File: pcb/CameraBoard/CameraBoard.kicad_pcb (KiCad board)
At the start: 2 copper layers, 17 parts, among them P2 CONN_01X03, P3 CONN_01X03, P4 CONN_01X08, U1 arduino_mini, U2 notgate_74HCT04

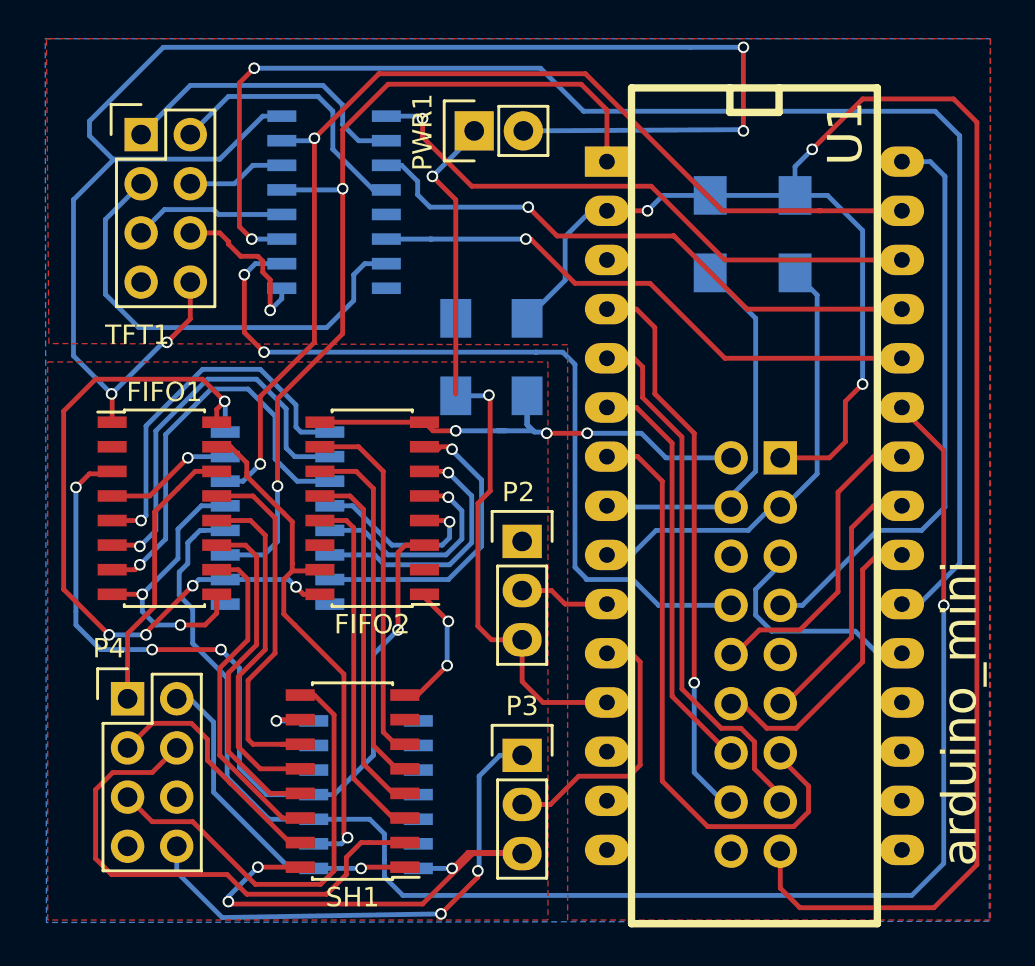
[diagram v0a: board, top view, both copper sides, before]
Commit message: moved camera board pcb to sub-folder
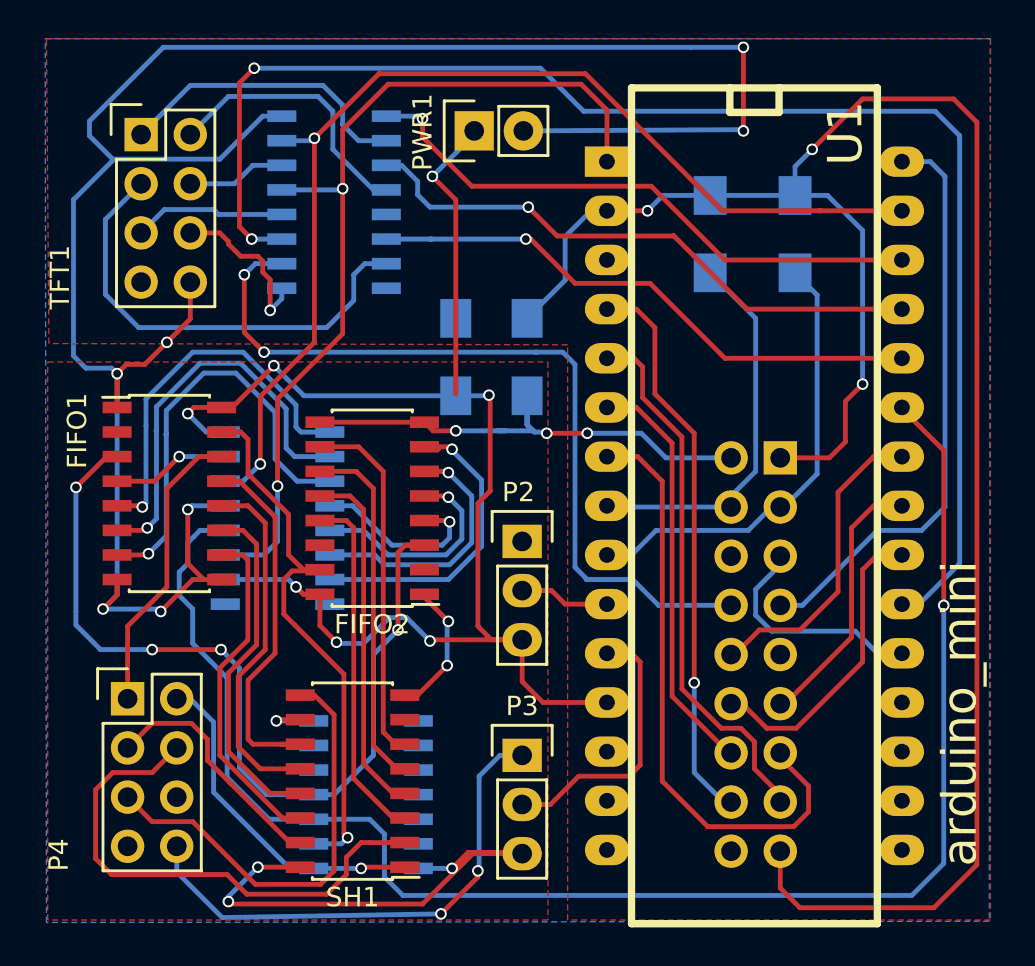
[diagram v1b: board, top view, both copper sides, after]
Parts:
- moved FIFO1 0.80 mm to (138.0, 110.2)
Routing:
- net GND: track 165.1 -> 177.9 mm, vias 14 -> 15
- net Net-(FIFO1-Pad15): track 27.7 -> 29.6 mm
- net Net-(FIFO1-Pad14): track 14.3 -> 15.3 mm
- net +5V: track 102.5 -> 101.7 mm
- net Net-(FIFO1-Pad7): track 21.7 -> 22.4 mm
- net Net-(FIFO1-Pad5): track 19.2 -> 19.9 mm
- net Net-(FIFO1-Pad10): track 17.5 -> 18.2 mm
- net Net-(FIFO1-Pad4): track 6.68 -> 6.11 mm
- net Net-(FIFO1-Pad3): track 44.7 -> 45.3 mm
- net Net-(FIFO1-Pad6): track 20.7 -> 21.2 mm

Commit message: fixed PCB
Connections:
- P4 pad 2: Net-(P4-Pad2) -> Net-(FIFO1-Pad15)
- SH1 pad 1: Net-(P4-Pad2) -> Net-(FIFO1-Pad15)
- U2 pad 1: Net-(P4-Pad2) -> (no net)
- U2 pad 2: Net-(FIFO1-Pad15) -> (no net)
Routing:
- net Net-(P4-Pad2): track 17.6 -> 0.00 mm, vias 1 -> 0
- net Net-(FIFO1-Pad15): track 29.6 -> 46.3 mm, vias 1 -> 2
